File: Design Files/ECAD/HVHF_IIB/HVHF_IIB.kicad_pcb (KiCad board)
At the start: 4 copper layers, 125 x 90 mm, 70 parts, among them J1 1984963, J2 1984963, J3 731375003, J4 CONSMA002-L, J5 1984963, Q1 PNP, Q2 BFP196E6327HTSA1, T1 BFU590G, T10 BFQ252, T11 BFQ252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

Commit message: fixed orientation error T4,T10-T12
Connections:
- R12 pad 2: Net-(T4-C) -> Net-(T4-E)
- R20 pad 2: Net-(T10-C) -> Net-(T10-E)
- R21 pad 2: Net-(T11-C) -> Net-(T11-E)
- R22 pad 2: Net-(T12-C) -> Net-(T12-E)
- T10 pad 1: GND -> Net-(T10-E)
- T10 pad 2: Net-(T10-C) -> GND
- T11 pad 1: GND -> Net-(T11-E)
- T11 pad 2: Net-(T11-C) -> GND
- T12 pad 1: GND -> Net-(T12-E)
- T12 pad 2: Net-(T12-C) -> unconnected-(T12-C-Pad2)
- T4 pad 1: GND -> Net-(T4-E)
- T4 pad 2: Net-(T4-C) -> GND
- T5 pad 1: Net-(T4-C) -> Net-(T4-E)
- T6 pad 1: Net-(T10-C) -> Net-(T10-E)
- T7 pad 1: Net-(T11-C) -> Net-(T11-E)
- T9 pad 1: Net-(T12-C) -> Net-(T12-E)
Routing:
- net Net-(T4-C): track 33.2 -> 0.00 mm
- net Net-(T11-E): track 0.00 -> 32.8 mm
- net Net-(T10-C): track 32.1 -> 0.00 mm
- net Net-(T12-C): track 31.9 -> 0.00 mm
- net Net-(T11-C): track 31.7 -> 0.00 mm
- net Net-(T10-E): track 0.00 -> 31.7 mm
- net Net-(T12-E): track 0.00 -> 31.5 mm
- net Net-(T4-E): track 0.00 -> 31.0 mm
- net GND: track 11.8 -> 15.6 mm
- net unconnected-(T12-C-Pad2): track 0.00 -> 1.52 mm

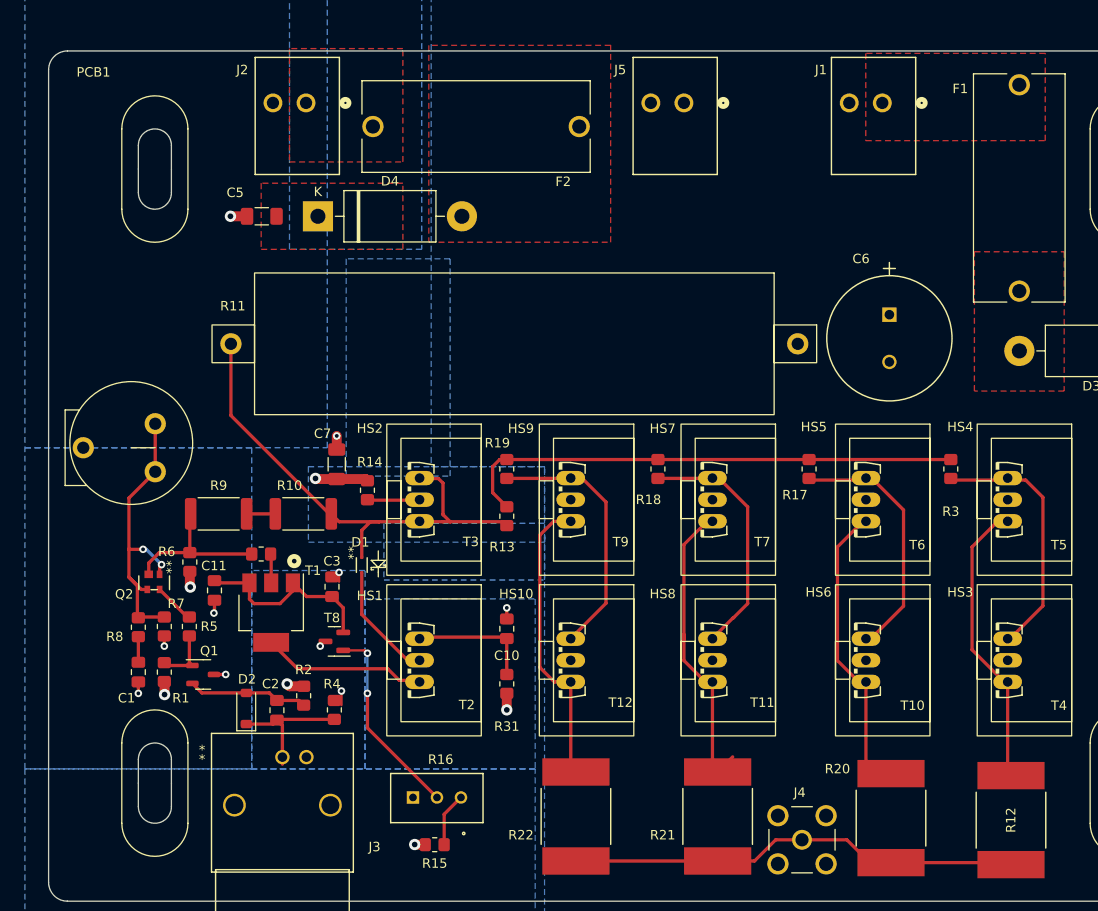
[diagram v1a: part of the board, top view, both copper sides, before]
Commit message: fixes, adds, silk
fixed Q1 rotation
adds LED
adds GND
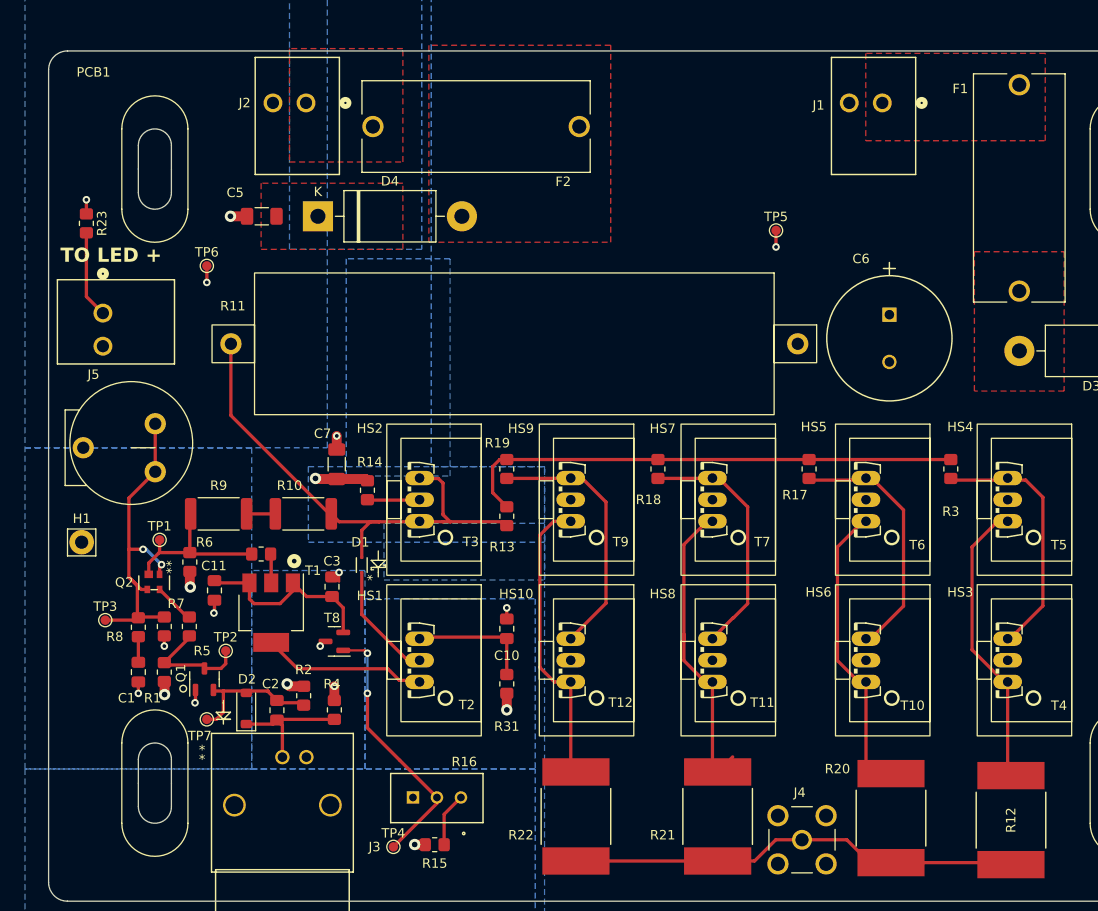
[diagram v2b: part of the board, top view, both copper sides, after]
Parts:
- added H1: MountingHole_Pad, Connector_Pin:Pin_D1.4mm_L8.5mm_W2.8mm_FlatFork, F.Cu at (91.0, 107.0)
- added R23: 360, Resistor_SMD:R_0805_2012Metric_Pad1.20x1.40mm_HandSolder, F.Cu at (91.5, 73.2)
- added TP1: TestPoint, TestPoint:TestPoint_Pad_D1.0mm, F.Cu at (99.2, 106.8)
- added TP2: TestPoint, TestPoint:TestPoint_Pad_D1.0mm, F.Cu at (106.2, 118.5)
- added TP3: TestPoint, TestPoint:TestPoint_Pad_D1.0mm, F.Cu at (93.5, 115.2)
- added TP4: TestPoint, TestPoint:TestPoint_Pad_D1.0mm, F.Cu at (124.0, 139.2)
- added TP5: TestPoint, TestPoint:TestPoint_Pad_D1.0mm, F.Cu at (164.5, 74.0)
- added TP6: TestPoint, TestPoint:TestPoint_Pad_D1.0mm, F.Cu at (104.2, 77.8)
- added TP7: TestPoint, TestPoint:TestPoint_Pad_D1.0mm, F.Cu at (104.2, 125.8)
- moved J5 64.3 mm to (93.2, 84.6), turned to -90 degrees
- moved Q1 0.52 mm to (104.0, 121.5), turned to 90 degrees
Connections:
- J5 pad 1: GND -> /LED
- Q1 pad 1: Net-(Q1-C) -> GND
- Q1 pad 3: GND -> Net-(Q1-E)
- R1 pad 2: Net-(Q1-C) -> Net-(Q1-E)
- R5 pad 1: Net-(Q1-C) -> Net-(Q1-E)
- T12 pad 2: unconnected-(T12-C-Pad2) -> GND
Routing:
- net Net-(Q1-E): track 0.00 -> 12.5 mm
- net /LED: track 0.00 -> 9.22 mm
- net Net-(T8-B): track 21.0 -> 28.1 mm
- net Net-(Q1-C): track 6.36 -> 0.00 mm
- net Net-(Q2-E): track 32.7 -> 36.5 mm
- net +5V: track 7.78 -> 11.0 mm, vias 5 -> 7
- net Net-(D2-A): track 12.7 -> 15.1 mm
- net +VDC: track 5.60 -> 7.35 mm, vias 1 -> 2
- net GND: track 15.6 -> 17.2 mm
- net unconnected-(T12-C-Pad2): track 1.52 -> 0.00 mm
- net /FB2: track 16.8 -> 18.1 mm
- net input: track 14.5 -> 13.7 mm
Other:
- board text added: "TO LED +"

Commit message: trace length matching
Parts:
- D2: renamed from D1; footprint Library:CR_BAS70-02V_INF-L -> Library:SOT-23_ONS
- moved D2 1.10 mm to (121.8, 109.4), turned to -90 degrees
- moved R3 1.00 mm to (184.0, 99.2)
- renumbered D2 to D1
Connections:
- D2 pad 1: Net-(D1-K) -> /FB1
- D2 pad 2: /FB1 -> (no net)
- T2 pad 2: Net-(D1-K) -> Net-(D2-K)
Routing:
- net Net-(R13-Pad1): track 53.7 -> 111.4 mm
- net Net-(D1-K): track 13.2 -> 0.00 mm
- net Net-(D2-K): track 0.00 -> 13.2 mm
- net Net-(T4-E): track 31.0 -> 33.7 mm
- net Net-(T10-B): track 27.0 -> 29.3 mm
- net Net-(T11-E): track 32.8 -> 30.9 mm
- net Net-(T12-E): track 31.5 -> 30.5 mm
- net Net-(T10-E): track 31.7 -> 32.7 mm
- net Net-(T12-B): track 28.4 -> 29.3 mm
- net Net-(T4-B): track 27.3 -> 26.5 mm
- net Net-(T11-B): track 26.3 -> 27.0 mm

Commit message: Post DR
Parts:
- removed HS1: ~, Library:ATS_PCB1025
- moved D2 16.0 mm to (110.3, 98.2), turned to 0 degrees
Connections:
- R11 pad 2: /FB1 -> Net-(D2-K)
- T3 pad 3: /FB1 -> Net-(D2-K)
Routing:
- net Net-(D2-K): track 13.2 -> 61.6 mm
- net /FB1: track 53.8 -> 30.9 mm
- net Net-(R13-Pad1): track 111.4 -> 99.7 mm
- net Net-(T4-B): track 26.5 -> 25.4 mm

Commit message: stitching done
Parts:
- added HS1: ~, Library:ATS_PCB1025, F.Cu at (127.3, 111.0)
- R12, R20, R21, R22: footprint Library:RES_3560_TEC -> Library:RES_ALSR05_VIS
- moved J2 49.6 mm to (162.5, 60.6)
- moved R15 37.5 mm to (94.0, 124.0)
- moved R16 37.5 mm to (91.7, 119.0)
- moved R12 35.2 mm to (155.0, 129.0), turned to 0 degrees
- moved TP4 34.3 mm to (91.0, 130.0)
- moved J4 24.8 mm to (192.0, 138.5)
- moved R20 21.8 mm to (155.0, 139.0), turned to 0 degrees
- moved TP1 15.7 mm to (103.0, 91.5)
- moved D4 13.8 mm to (113.4, 59.0)
- moved D2 11.7 mm to (113.8, 87.0)
- moved F2 11.4 mm to (144.0, 61.0), turned to 0 degrees
- moved C7 11.2 mm to (120.0, 87.7)
- moved R22 10.4 mm to (151.0, 129.0), turned to 180 degrees
- moved D3 9.54 mm to (202.0, 95.6), turned to 90 degrees
- moved C1 8.94 mm to (96.0, 111.9)
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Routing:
- net Net-(T8-B): track 28.1 -> 83.5 mm
- net Net-(T4-E): track 33.4 -> 84.9 mm
- net Net-(T11-E): track 30.9 -> 70.9 mm
- net Net-(T12-E): track 30.5 -> 69.8 mm
- net Net-(T10-E): track 32.7 -> 70.0 mm
- net output: track 48.1 -> 65.4 mm
- net input: track 13.7 -> 22.0 mm
- net /FB2: track 18.1 -> 21.1 mm
- net Net-(D2-K): track 61.6 -> 58.7 mm
- net /FB1: track 30.9 -> 29.0 mm
- net Net-(Q2-E): track 36.5 -> 34.9 mm
- net GND: track 17.2 -> 18.5 mm, vias 10 -> 86
- net +VDC: track 7.35 -> 7.98 mm
- added copper zone on B.Cu, net /+5V_IN
- added copper zone on F.Cu, net GND

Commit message: checked footprints
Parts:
- Q1: footprint Package_TO_SOT_SMD:SOT-23-3 -> Library:SOT-23_ONS
- T8: footprint Package_TO_SOT_SMD:SOT-23 -> Library:SOT23_NXP
- turned Q1 to 0 degrees
- turned T8 to 90 degrees
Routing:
- net +VDC: track 7.98 -> 5.98 mm
- net GND: track 18.5 -> 19.8 mm, vias 86 -> 99

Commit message: JLC SUBMIT 6/17/2024
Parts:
- C11, C3: value 100n -> 0.1u
- D1: footprint Diode_SMD:D_SOD-123 -> Library:SOD123_MCC-M
- J1, J2, J5: footprint 1_My_Custom_Library:CONN_1984963 -> Library:CONN_1984963
- R10, R9: footprint Resistor_SMD:R_2512_6332Metric -> Library:RC2512N_VIS-M
- moved LOGO1 16.7 mm to (132.5, 72.5)
- moved TP5 2.38 mm to (168.5, 70.2)
- moved C3 0.50 mm to (116.0, 102.8)
- moved C11 0.44 mm to (104.5, 103.2)
- moved J4 0.34 mm to (192.0, 138.8)
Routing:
- net Net-(T4-E): track 84.9 -> 74.9 mm
- net /FB1: track 29.0 -> 27.9 mm
- net +VDC: track 5.98 -> 7.01 mm
- net Net-(T1-E): track 20.7 -> 21.3 mm
- net GND: track 19.8 -> 20.1 mm, vias 99 -> 234
- removed copper zone on B.Cu, net /+5V_IN
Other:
- board text added: "*"
